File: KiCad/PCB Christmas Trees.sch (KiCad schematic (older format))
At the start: 36 parts

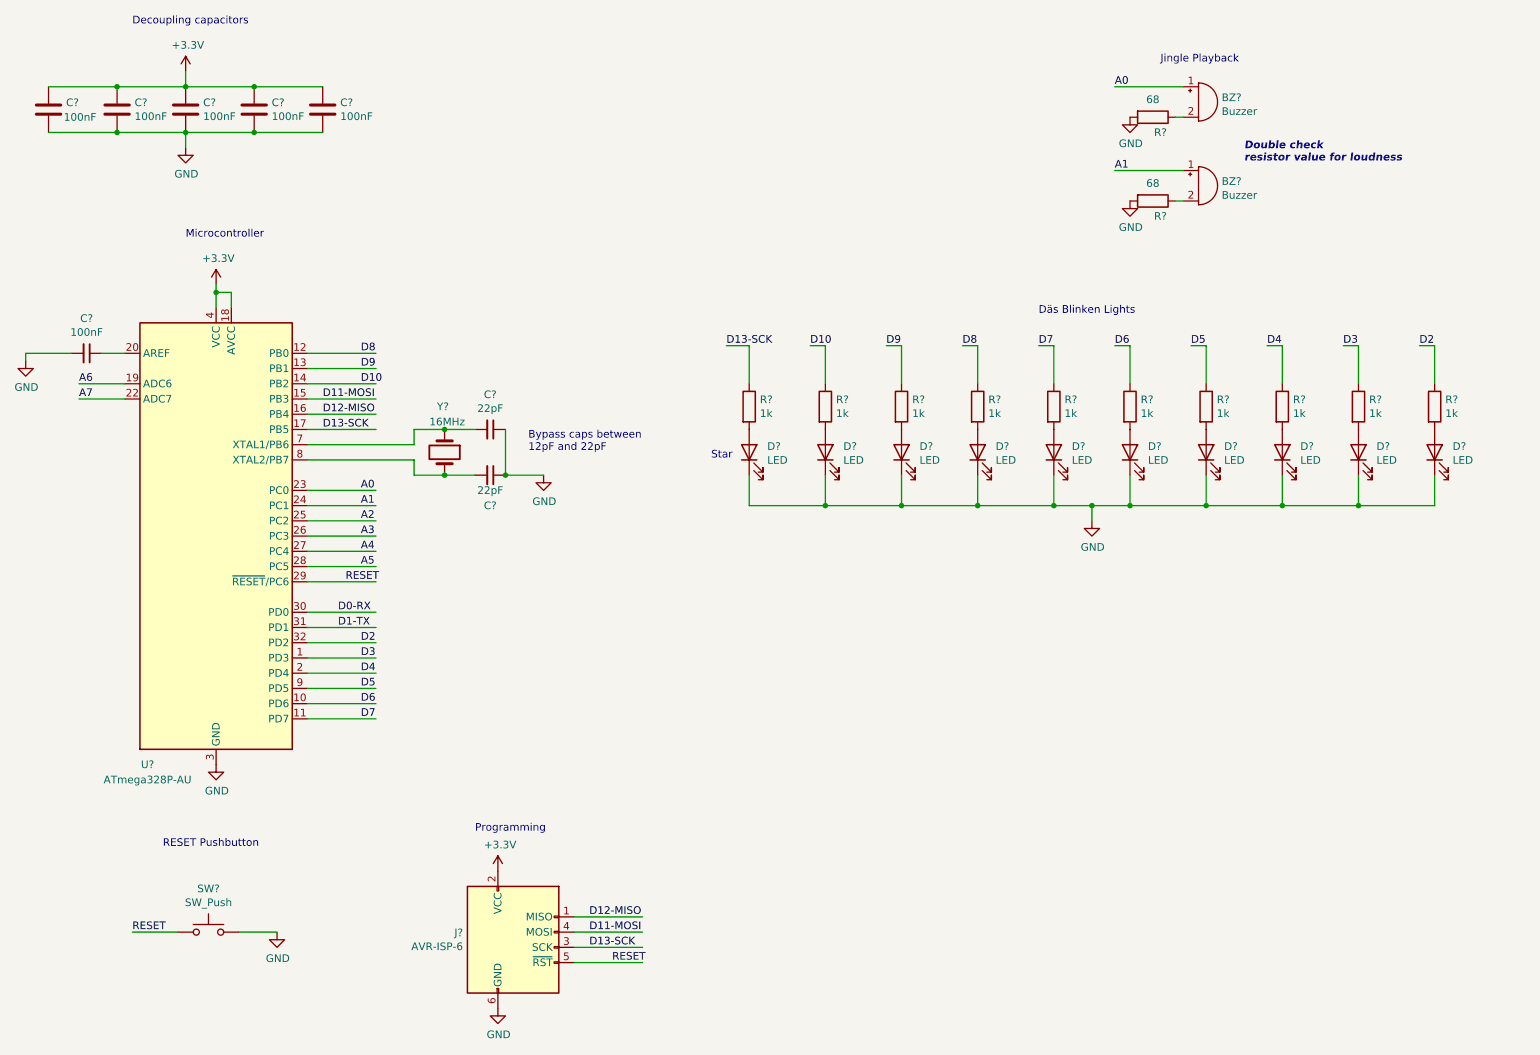
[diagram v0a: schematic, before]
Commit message: Touch sensetive ornaments added
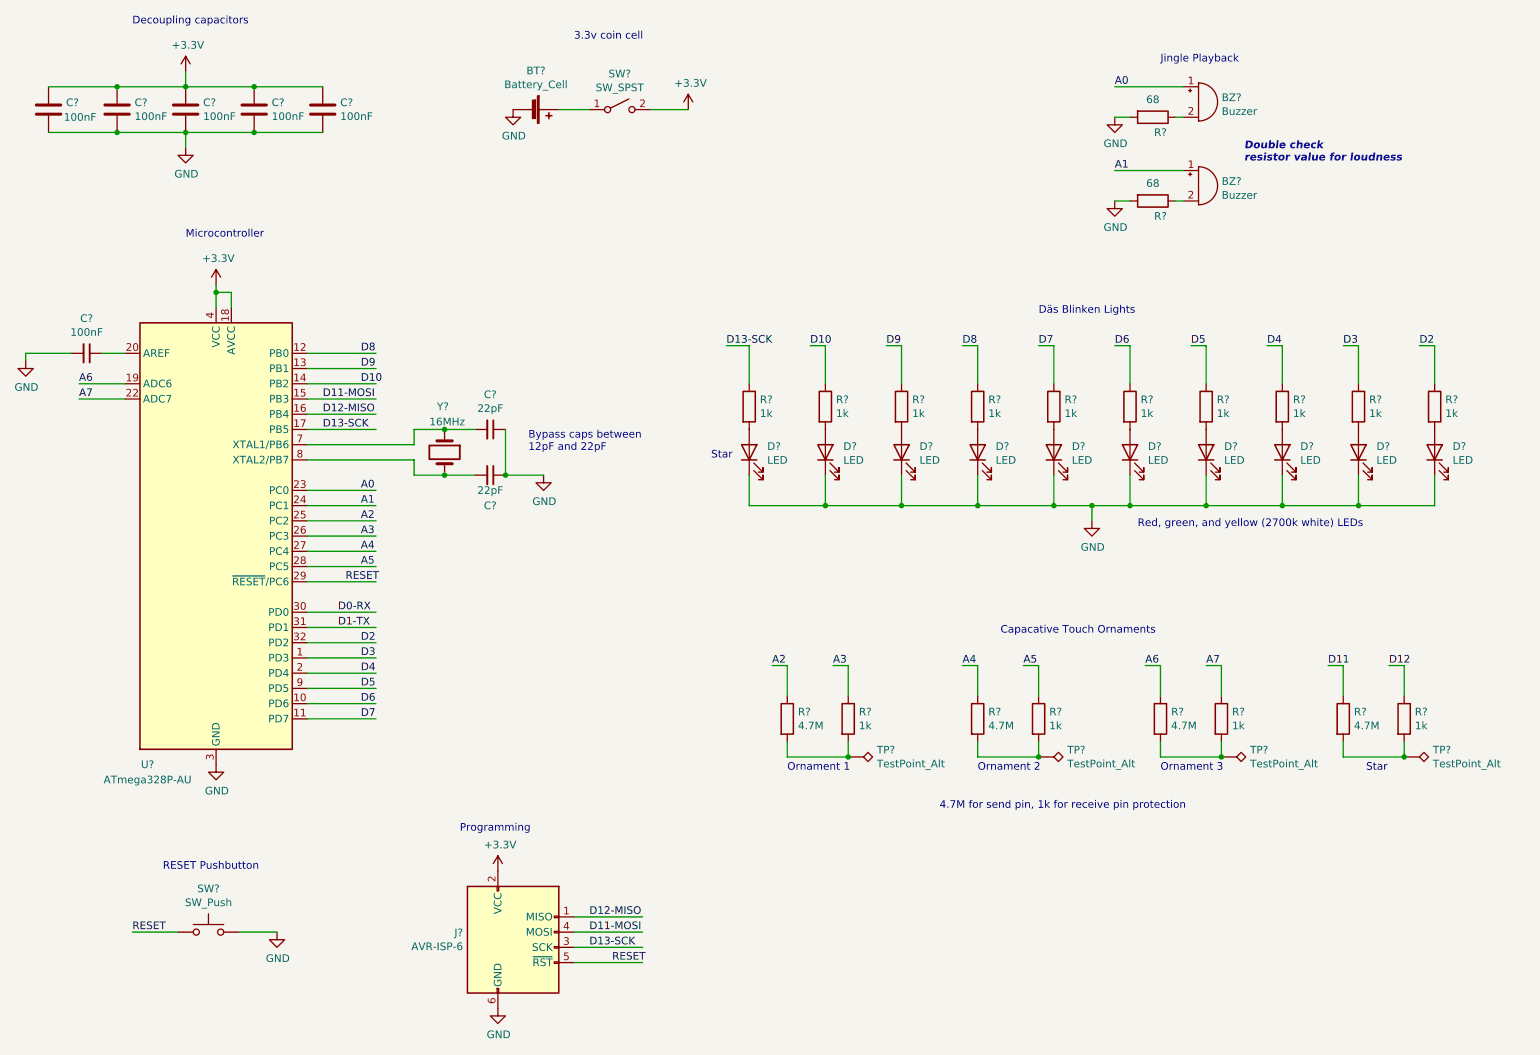
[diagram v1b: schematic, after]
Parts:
- added BT?: Battery_Cell, symbol Device:Battery_Cell
- added R? (x4): 4.7M, symbol Device:R
- added R? (x4): 1k, symbol Device:R
- added SW?: SW_SPST, symbol Switch:SW_SPST
- added TP? (x4): TestPoint_Alt, symbol Connector:TestPoint_Alt
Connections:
- net labels added: D11, D12
- wire segments 101 -> 133
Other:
- note added: "3.3v coin cell"
- note added: "4.7M for send pin, 1k for receive pin protection"
- note added: "Capacative Touch Ornaments"
- note added: "Ornament 1"
- note added: "Ornament 2\n"
- note added: "Ornament 3"
- note added: "Red, green, and yellow (2700k white) LEDs"

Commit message: More updates
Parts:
- added C? (x4): 100 pF, symbol Device:C_Small
- added R?: 1k, symbol Device:R
- added SW?: SW_Push, symbol Switch:SW_Push
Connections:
- net labels added: D1
- wire segments 133 -> 140
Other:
- note added: "LED Mode Change\n"
- moved on the sheet: R?, TP?

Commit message: More changes....
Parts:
- BT1: renamed from BT?; value Battery_Cell -> CR2032
- gave numbers to parts that had none: 55
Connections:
- wire segments 140 -> 138

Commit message: Finally done with the schematic! (I think...)
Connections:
- net labels removed: D1, D11, D12
- wire segments 138 -> 141
- no-connect marks 0 -> 1
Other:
- moved on the sheet: C12
